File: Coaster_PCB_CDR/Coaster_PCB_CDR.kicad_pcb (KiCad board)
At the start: 2 copper layers, 99.5 x 99 mm, 34 parts, among them J1 Vin, J10 GND, J12 GND, J13 3v3, J15 GND, J16 GND, J17 GND, J2 HC-05, J3 10V, J4 Batt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

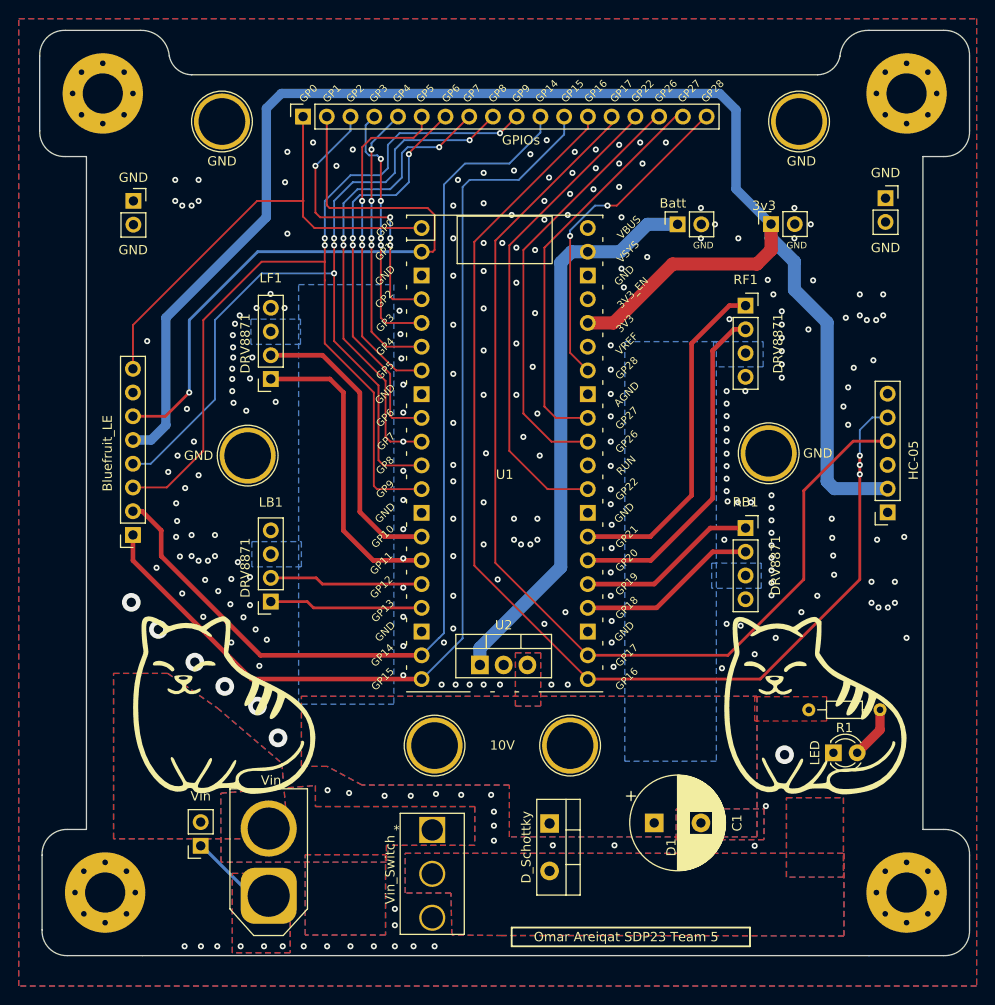
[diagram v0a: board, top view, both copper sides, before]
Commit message: flipped hc05
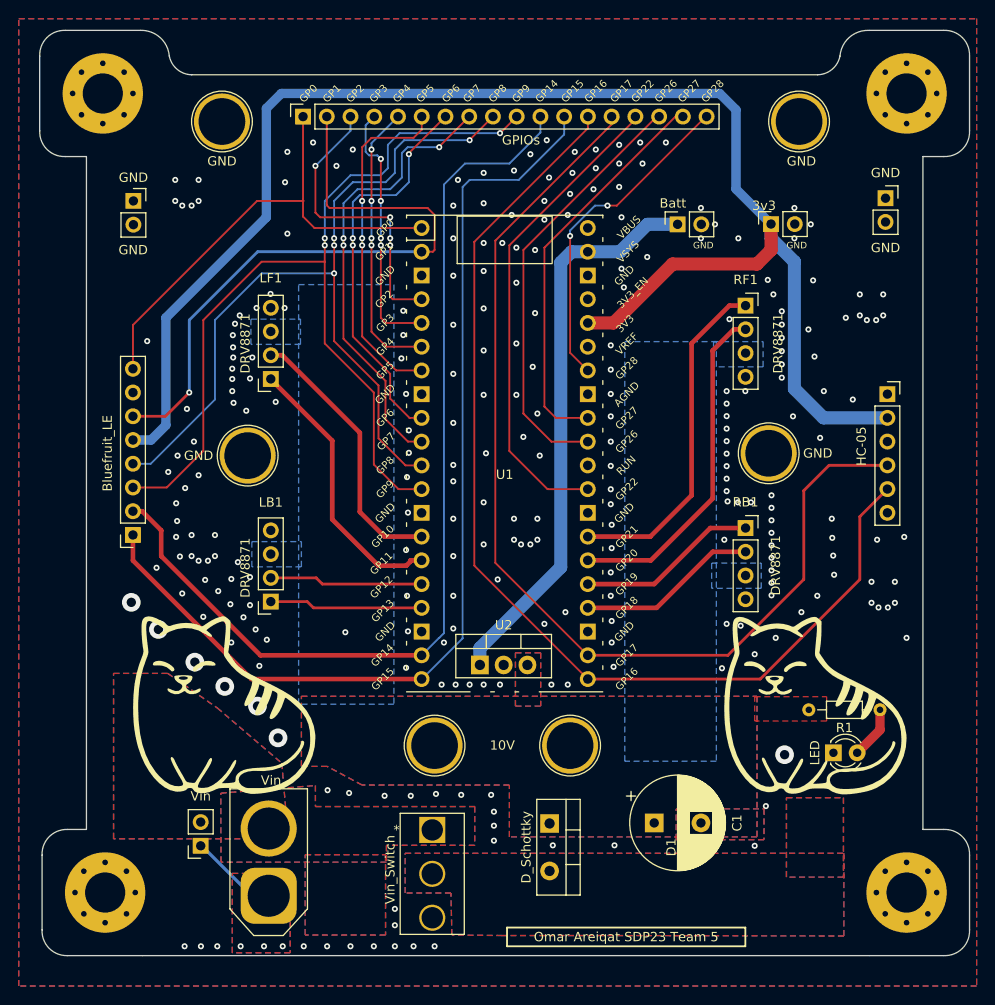
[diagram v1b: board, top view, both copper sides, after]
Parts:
- moved J2 12.7 mm to (167.7, 96.4), turned to 0 degrees
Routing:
- net GPIO16: track 125.3 -> 114.7 mm, vias 3 -> 0
- net +3V3: track 170.4 -> 163.5 mm
- net LF1: track 32.8 -> 29.7 mm
- net LF2: track 31.7 -> 29.1 mm
- net GPIO8: track 92.5 -> 91.1 mm
- net GPIO9: track 103.1 -> 101.8 mm
- net GPIO7: track 50.6 -> 49.4 mm
- net GPIO17: track 114.0 -> 112.9 mm
- net GPIO6: track 44.3 -> 43.2 mm
- net GND: vias 273 -> 272

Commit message: added more ground
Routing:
- net GND: vias 272 -> 274

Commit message: xx
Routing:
- net +3V3: track 163.5 -> 178.1 mm
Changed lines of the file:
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@@
   (segment (start 138.4 88.8075) (end 144.7075 82.5) (width 1.4) (layer "F.Cu") (net 15))
   (segment (start 90.5 88.25) (end 101.25 77.5) (width 1) (layer "B.Cu") (net 15))
+  (segment (start 152.15 82.25) (end 157.75 82.25) (width 1) (layer "B.Cu") (net 15))
+  (segment (start 151.5 74.475) (end 150.3 75.675) (width 1) (layer "B.Cu") (net 15))
   (segment (start 151.5 66) (end 151.5 74.475) (width 1) (layer "B.Cu") (net 15))
   (segment (start 149.75 64.25) (end 151.5 66) (width 1) (layer "B.Cu") (net 15))
@@
   (segment (start 167.7 98.96) (end 160.86 98.96) (width 1.4) (layer "B.Cu") (net 15))
   (segment (start 88.92 101.33) (end 90.5 99.75) (width 1) (layer "B.Cu") (net 15))
+  (segment (start 150.3 75.675) (end 150.3 80.4) (width 1) (layer "B.Cu") (net 15))
   (segment (start 157.75 82.25) (end 155.25 79.75) (width 1.4) (layer "B.Cu") (net 15))
+  (segment (start 150.3 80.4) (end 152.15 82.25) (width 1) (layer "B.Cu") (net 15))
   (segment (start 155.25 79.75) (end 155.25 78.225) (width 1.4) (layer "B.Cu") (net 15))
   (segment (start 86.975 101.33) (end 88.92 101.33) (width 1) (layer "B.Cu") (net 15))

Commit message: changed pcb
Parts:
- removed J10, J12, J15, J5: GND, TestPoint:TestPoint_Plated_Hole_D5.0mm
- added J18: 5v, Connector_PinSocket_2.54mm:PinSocket_1x02_P2.54mm_Vertical, F.Cu at (167.4, 79.3)
- added J19: 5v, Connector_PinSocket_2.54mm:PinSocket_1x02_P2.54mm_Vertical, F.Cu at (156.9, 69.5)
- J9: value Bluefruit_LE -> 3v3; footprint Connector_PinSocket_2.54mm:PinSocket_1x08_P2.54mm_Vertical -> Connector_PinSocket_2.54mm:PinSocket_1x02_P2.54mm_Vertical
- R1: footprint Resistor_THT:R_Axial_DIN0204_L3.6mm_D1.6mm_P7.62mm_Horizontal -> Resistor_THT:R_Axial_DIN0309_L9.0mm_D3.2mm_P12.70mm_Horizontal
- moved J9 81.4 mm to (154.7, 66.4), turned to -90 degrees
- moved J17 15.6 mm to (164.3, 90.8), turned to 90 degrees
- moved D3 2.26 mm to (160.3, 136.4)
- moved R1 1.75 mm to (168.3, 129.2)
- moved J2 1.04 mm to (168.7, 96.6)
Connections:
- net Vcc_10v renamed VCC_Batt
- C1 pad 1: +10V -> vBatt
- D1 pad 1: +10V -> vBatt
- H1 pad 1: GND -> unconnected-(H1-Pad1)
- H2 pad 1: GND -> unconnected-(H2-Pad1)
- H3 pad 1: GND -> unconnected-(H3-Pad1)
- H4 pad 1: GND -> unconnected-(H4-Pad1)
- J2 pad 2: +3V3 -> VSYS
- J2 pad 4: GPIO17 -> GPIO16
- J2 pad 5: GPIO16 -> GPIO17
- J3 pad 1: +10V -> vBatt
- J7 pad 1: +10V -> vBatt
- J9 pad 1: GPIO15 -> +3V3
- J9 pad 2: CTS -> GND
- LB1 pad 3: +10V -> vBatt
- LF1 pad 3: +10V -> vBatt
- R1 pad 2: +10V -> vBatt
- RB1 pad 3: +10V -> vBatt
- RF1 pad 3: +10V -> vBatt
- U2 pad 1: VSYS -> vBatt
- U2 pad 3: +10V -> VSYS
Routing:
- net +3V3: track 178.1 -> 37.7 mm
- net VSYS: track 60.8 -> 149.0 mm
- net GPIO1: track 69.4 -> 26.7 mm, vias 1 -> 0
- net CTS: track 104.6 -> 65.7 mm
- net GPIO15: track 108.5 -> 69.6 mm
- net GPIO9: track 101.8 -> 63.1 mm
- net GPIO8: track 91.1 -> 56.1 mm, vias 4 -> 3
- net DFU: track 52.4 -> 23.9 mm
- net GPIO16: track 114.7 -> 118.8 mm
- net Net-(D3-Pad2): track 5.61 -> 9.47 mm
- net GPIO17: track 112.9 -> 110.7 mm
- net GND: vias 274 -> 195
- added copper zone on B.Cu, net vBatt
- added copper zone on F.Cu, net vBatt
- removed copper zone on B.Cu, net +10V
- removed copper zone on F.Cu, net +10V

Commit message: Updated PCB for FDR
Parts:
- removed J16, J17: GND, Connector_PinSocket_2.54mm:PinSocket_1x02_P2.54mm_Vertical
- removed Qat (x4): LOGO, Coaster_PCB_CDR:pic22
- added J10: 5v_Cap, Connector_PinSocket_2.54mm:PinSocket_1x02_P2.54mm_Vertical, F.Cu at (126.5, 66.8)
- added J11: GPIO_14-15, Connector_PinSocket_2.54mm:PinSocket_1x02_P2.54mm_Vertical, F.Cu at (84.8, 118.8)
- added J12: GPIO_27-28, Connector_PinSocket_2.54mm:PinSocket_1x02_P2.54mm_Vertical, F.Cu at (168.3, 83.1)
- added J5: HC-05, Connector_PinSocket_2.54mm:PinSocket_1x06_P2.54mm_Vertical, F.Cu at (84.5, 94.6)
- J4: value Batt -> Vsys_Cap
- J8: value GPIOs -> GPIO_0-1; footprint Connector_PinSocket_2.54mm:PinSocket_1x18_P2.54mm_Vertical -> Connector_PinSocket_2.54mm:PinSocket_1x02_P2.54mm_Vertical
- R1: footprint Resistor_THT:R_Axial_DIN0309_L9.0mm_D3.2mm_P12.70mm_Horizontal -> Resistor_THT:R_Axial_DIN0204_L3.6mm_D1.6mm_P7.62mm_Horizontal
- moved J18 73.1 mm to (95.4, 66.7)
- moved J9 49.7 mm to (105.0, 66.7), turned to 0 degrees
- moved J8 23.9 mm to (84.5, 78.6), turned to 0 degrees
- moved J4 12.6 mm to (140.0, 66.8), turned to 0 degrees
- moved J13 11.8 mm to (152.4, 66.7), turned to 0 degrees
- moved J19 4.61 mm to (160.5, 66.7), turned to 0 degrees
- moved D3 1.13 mm to (159.9, 137.4)
- moved R1 0.62 mm to (168.4, 129.8)
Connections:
- net DFU renamed GPIO0
- U1 pad 19: CTS -> GPIO14
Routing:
- net VSYS: track 149.0 -> 272.9 mm
- net CTS: track 65.7 -> 0.00 mm
- net GPIO9: track 63.1 -> 0.00 mm, vias 3 -> 0
- net GPIO8: track 56.1 -> 0.00 mm, vias 3 -> 0
- net GPIO22: track 51.2 -> 0.00 mm
- net GPIO7: track 49.4 -> 0.00 mm, vias 3 -> 0
- net GPIO16: track 118.8 -> 165.0 mm, vias 0 -> 2
- net GPIO26: track 45.8 -> 0.00 mm
- net GPIO6: track 43.2 -> 0.00 mm, vias 3 -> 0
- net GPIO17: track 110.7 -> 152.3 mm
- net +3V3: track 37.7 -> 78.0 mm
- net GPIO5: track 37.4 -> 0.00 mm, vias 3 -> 0
- net GPIO14: track 0.00 -> 35.4 mm
- net GPIO15: track 69.6 -> 35.4 mm
- net GPIO2: track 32.8 -> 0.00 mm, vias 4 -> 0
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- added copper zone on B.Cu, net VSYS
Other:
- board text removed: "GP0"
- board text removed: "GP1"
- board text removed: "GP14"
- board text removed: "GP15"
- board text removed: "GP16"
- board text removed: "GP17"
- board text removed: "GP2"
- board text removed: "GP22"
- board text removed: "GP26"
- board text removed: "GP27"
- board text removed: "GP28"
- board text removed: "GP3"
- board text removed: "GP4"
- board text removed: "GP5"
- board text removed: "GP6"
- board text removed: "GP7"
- board text removed: "GP8"
- board text removed: "GP9"

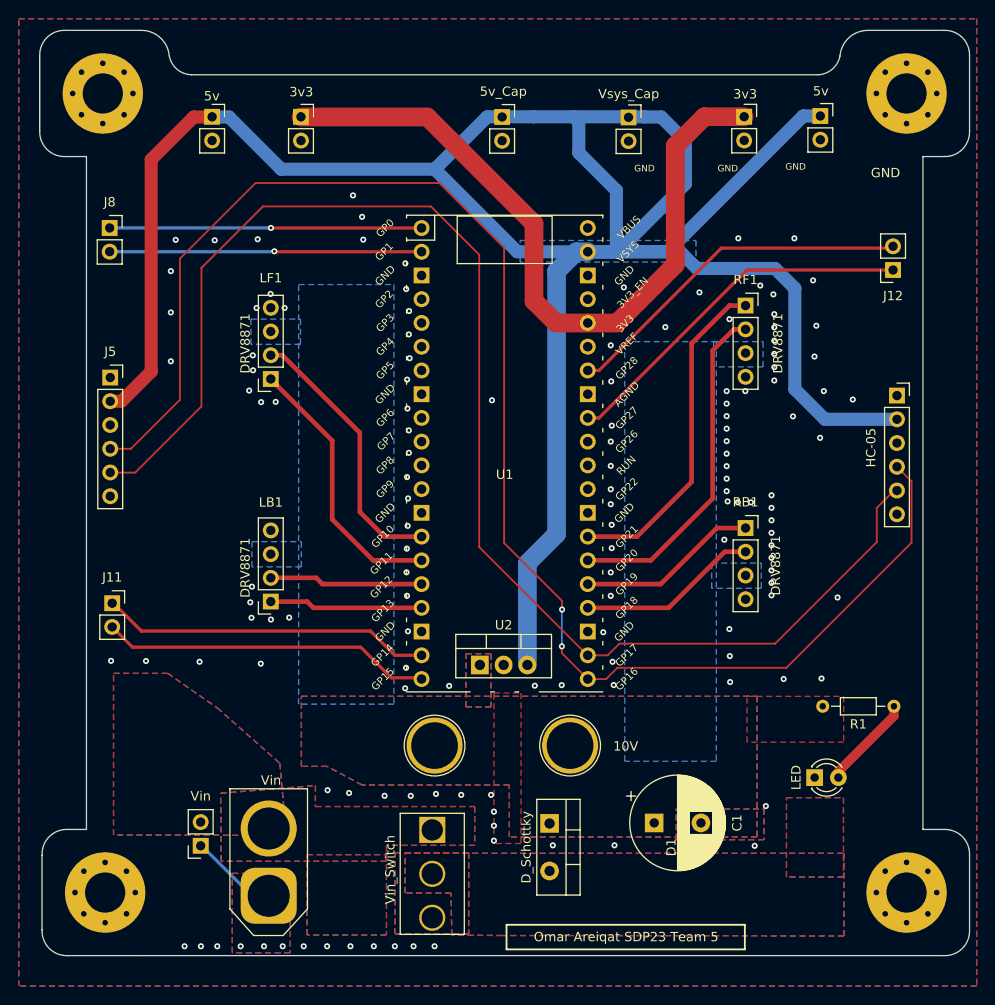
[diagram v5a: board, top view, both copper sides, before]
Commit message: modified gnd vias
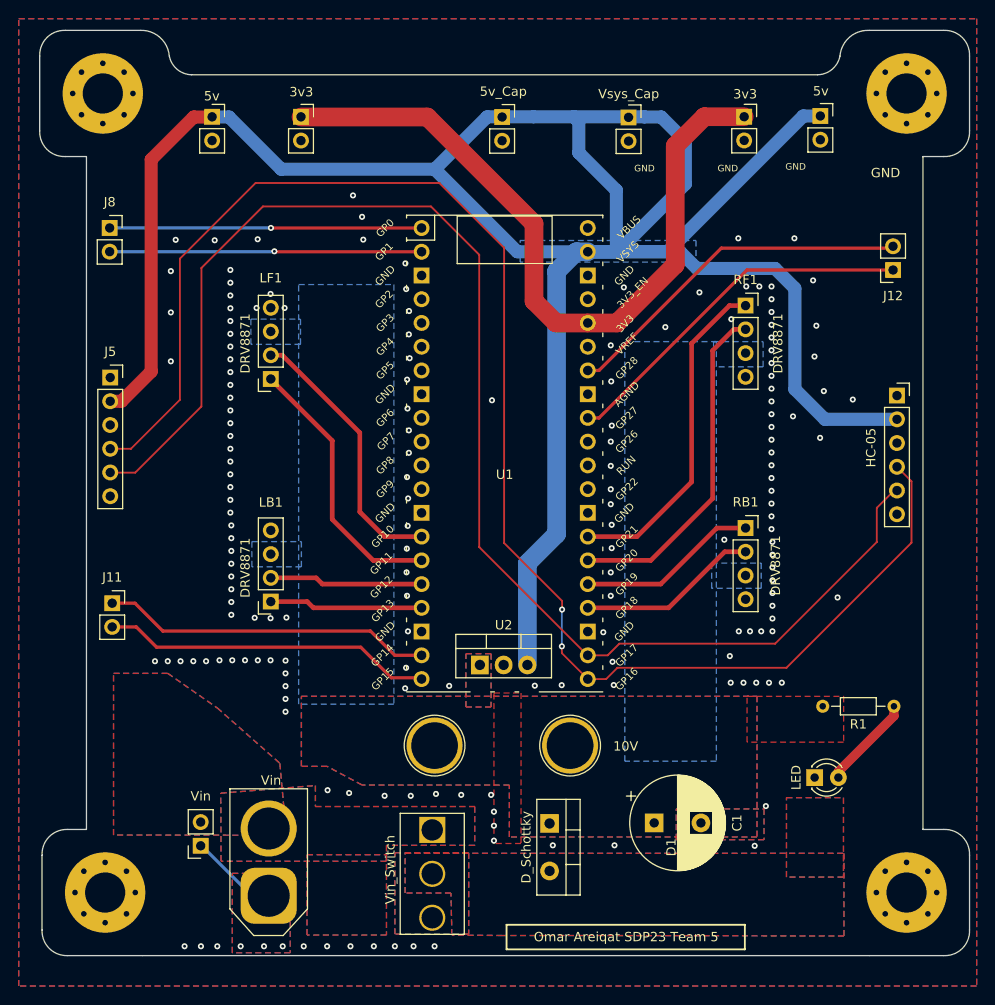
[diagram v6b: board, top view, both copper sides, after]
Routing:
- net GND: vias 139 -> 175

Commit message: decent amount of changes to board
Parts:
- added C2: 2200uF, Capacitor_THT:CP_Radial_D10.0mm_P5.00mm, F.Cu at (106.6, 133.3)
- J10: value 5v_Cap -> 5v
- J3: value 10V -> 14.8v
- J4: value Vsys_Cap -> 5v
- J7: value 10V -> VCC_Batt
- moved J7 42.5 mm to (158.7, 149.8)
- moved D3 16.0 mm to (165.6, 122.5), turned to -90 degrees
- moved J5 14.6 mm to (84.0, 109.2), turned to 180 degrees
- moved D1 14.5 mm to (146.1, 141.6)
- moved C1 13.2 mm to (152.5, 133.3)
- moved J3 10.8 mm to (144.5, 134.6)
- moved SW1 7.41 mm to (126.4, 142.7)
- moved J4 7.06 mm to (133.0, 66.2)
- moved J10 6.55 mm to (120.0, 66.2)
- moved J13 6.41 mm to (146.0, 66.1)
- moved J1 6.36 mm to (95.2, 149.2), turned to 0 degrees
- moved R1 4.86 mm to (165.6, 133.8), turned to -90 degrees
- moved J6 4.75 mm to (97.3, 141.2), turned to 90 degrees
- moved J12 2.18 mm to (169.2, 81.2)
- moved J9 2.07 mm to (106.9, 66.2)
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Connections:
- J2 pad 4: GPIO16 -> GPIO17
- J2 pad 5: GPIO17 -> GPIO16
- J7 pad 1: vBatt -> VCC_Batt
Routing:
- net GND: track 9.49 -> 0.00 mm, vias 175 -> 138
- net GPIO16: track 165.0 -> 155.9 mm, vias 2 -> 0
- net VSYS: track 272.9 -> 265.1 mm
- net +3V3: track 78.0 -> 70.9 mm
- net GPIO28: track 38.2 -> 39.9 mm
- net GPIO27: track 39.2 -> 40.9 mm
- net Net-(D3-Pad2): track 10.1 -> 8.62 mm
- net GPIO17: track 152.3 -> 153.5 mm
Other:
- board text added: "5v"
- board text added: "GP0"
- board text added: "GP1"
- board text added: "GP14"
- board text added: "GP15"
- board text added: "GP16"
- board text added: "GP17"
- board text added: "GP27"
- board text added: "GP28"
